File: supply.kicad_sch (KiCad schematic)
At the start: 138 parts, among them J10002 PinHeader_1x3_P2.54mm_Drill1.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, J1001 BarrelJack_3167288, Q10001 BSS138PW, Q1001 SI7613DN-T1-GE3, Q1002 BSS138PW, SW1001 SW_CVS-02B, U10001 NCP718BSN330T1G, U10002 MPM54304GMN, U10003 MPM54304GMN, U10004 MAX16150A_SOT, U10006 LM3880, U10007 MP8869S, U10008 XC6230H001ER-G, U10009 MAX812REUS+T, U1001 LTC4412IS6, U10010 PAC1954T-E_VQFN, U10011 PAC1954T-E_VQFN

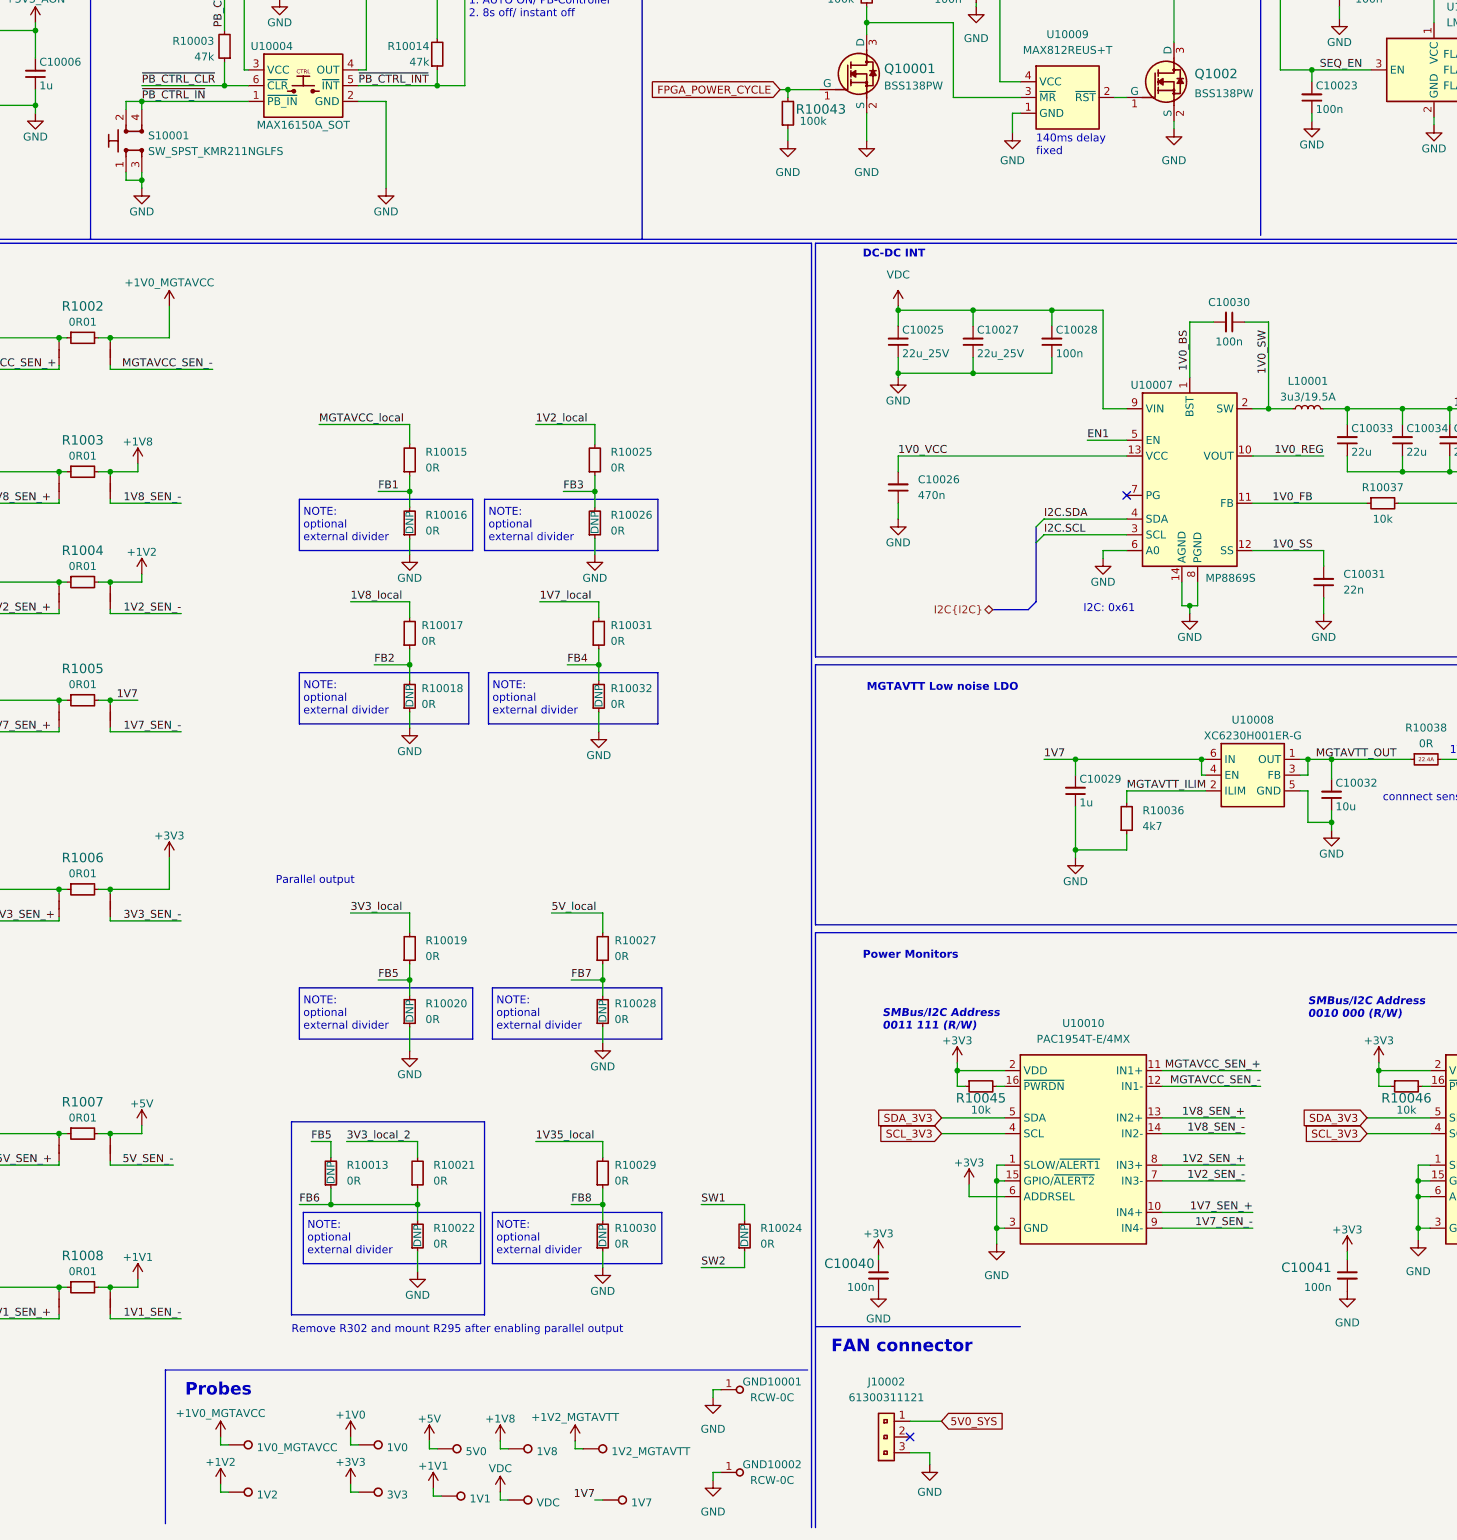
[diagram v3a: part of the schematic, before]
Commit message: Sync Supply sheet with PCB
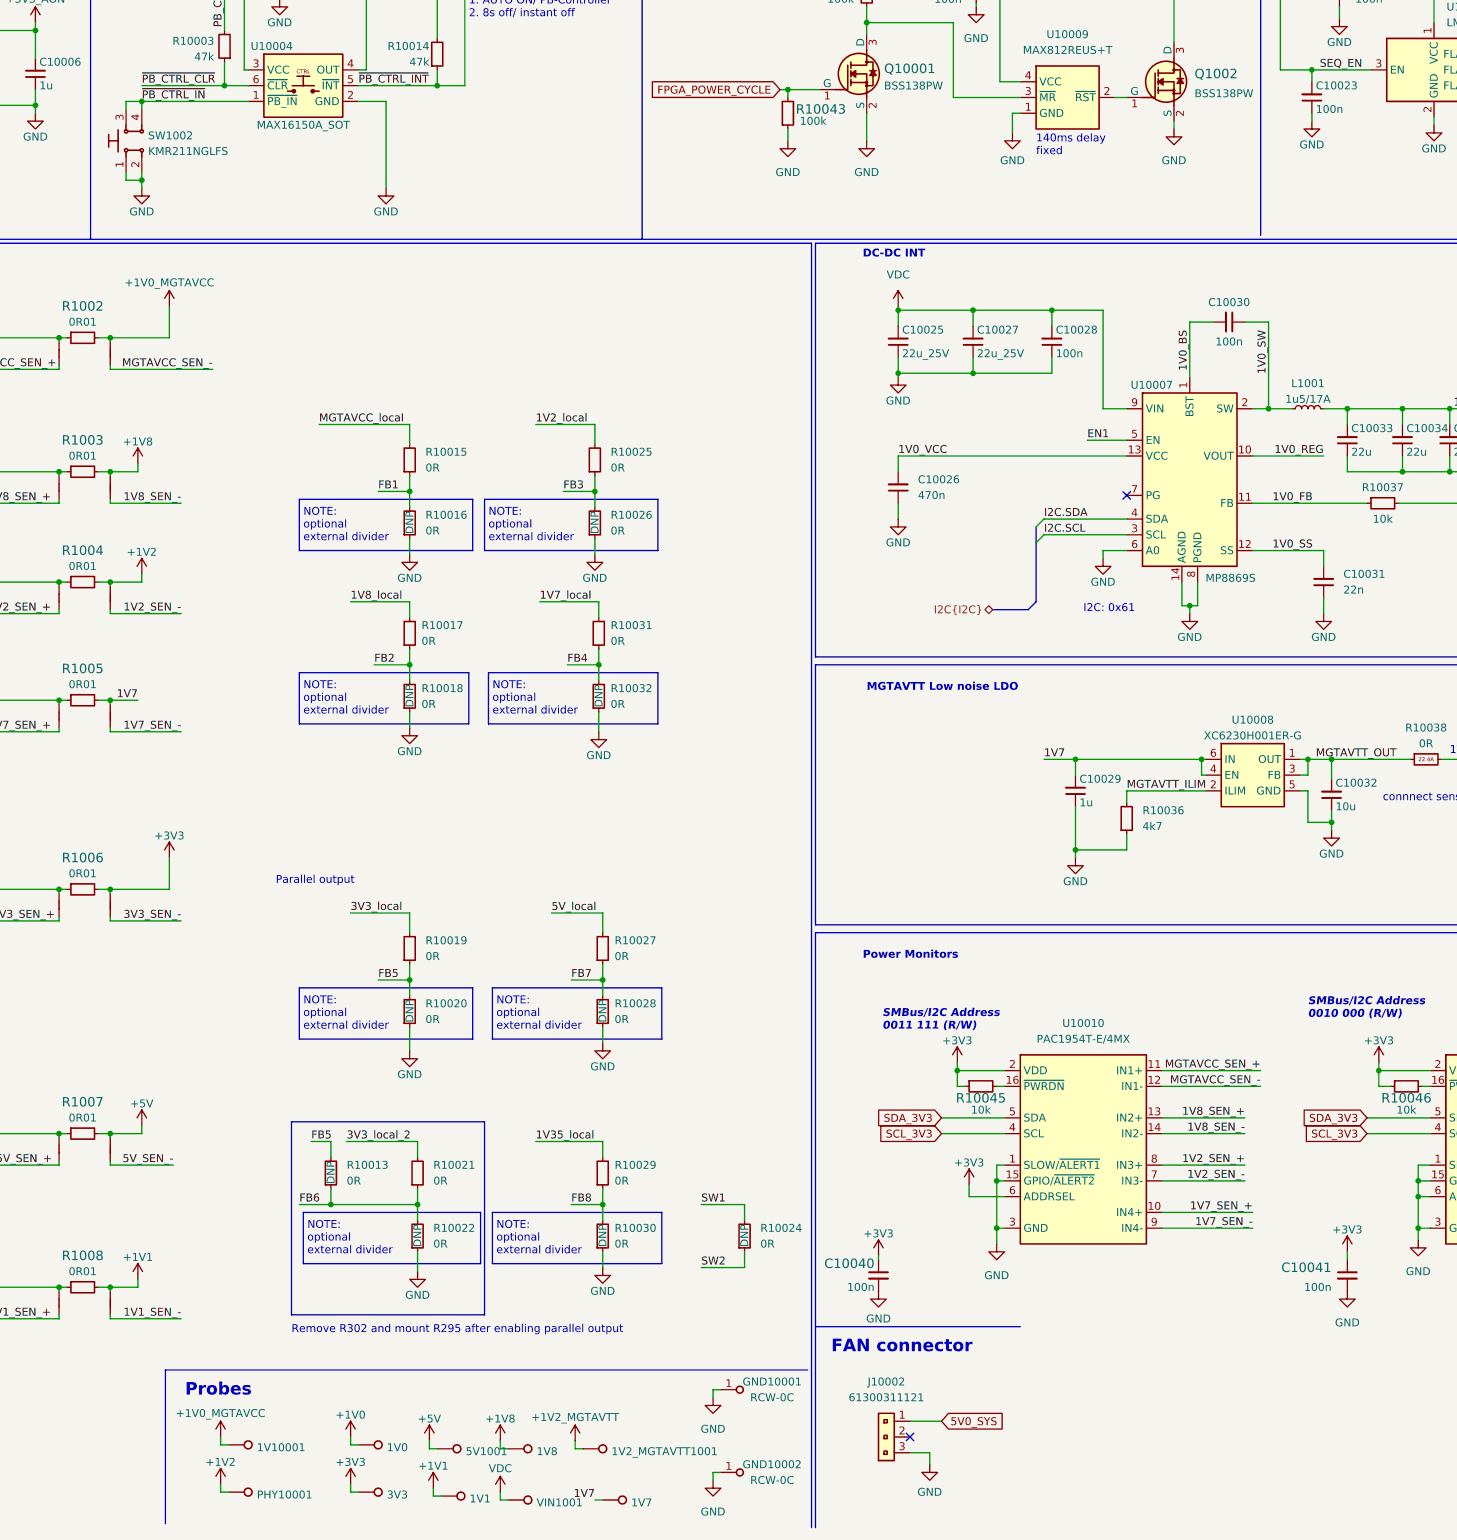
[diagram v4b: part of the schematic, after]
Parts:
- removed L10001: SRP6050CA-1R5M, K410T-devboard-footprints:Bourns-SRP6050CA, symbol K410T-devboard:SRP6050CA-1R5M
- removed S10001: SW_SPST_KMR211NGLFS, K410T-devboard-footprints:SW_SPST_4.2x2.8, symbol K410T-devboard:SW_SPST_KMR211NGLFS
- added L1001: L_1u5_17A_Bourns-SRP6050CA, antmicro-footprints:L_Bourns-SRP6050CA, symbol antmicroFixedInductors:L_1u5_17A_Bourns-SRP6050CA
- added SW1002: SW_KMR211NGLFS_SMD, antmicro-footprints:SW_KMR211NGLFS_SMD, symbol antmicroPushbuttonSwitches:SW_KMR211NGLFS_SMD
- renumbered 1V0_MGTAVCC to 1V10001, 1V2_MGTAVTT to 1V2_MGTAVTT1001, 5V0 to 5V1001, 1V2 to PHY10001, VDC to VIN1001
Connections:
- net 1V0_REG: now also L1001.2
- net 1V0_SW: now also L1001.1
- net GND: now also SW1002.1, SW1002.2
- net ~{PB_CTRL_IN}: now also SW1002.3, SW1002.4
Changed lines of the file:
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@@
   (symbol (lib_id "data-center-rdimm-ddr4-tester:TP_1mm_SMD") (at 205.74 272.415 0) (unit 1)
     (in_bom yes) (on_board yes) (fields_autoplaced)
-    (property "Reference" "5V0" (id 0) (at 210.312 272.8488 0)
+    (property "Reference" "5V1001" (id 0) (at 210.312 272.8488 0)
       (effects (font (size 1.27 1.27)) (justify left))
     )
@@
   (symbol (lib_id "data-center-rdimm-ddr4-tester:TP_1mm_SMD") (at 172.085 279.4 0) (unit 1)
     (in_bom yes) (on_board yes) (fields_autoplaced)
-    (property "Reference" "1V2" (id 0) (at 176.657 279.8338 0)
+    (property "Reference" "PHY10001" (id 0) (at 176.657 279.8338 0)
       (effects (font (size 1.27 1.27)) (justify left))
     )
@@
   (symbol (lib_id "data-center-rdimm-ddr4-tester:TP_1mm_SMD") (at 217.17 280.67 0) (unit 1)
     (in_bom yes) (on_board yes)
-    (property "Reference" "VDC" (id 0) (at 221.742 281.1038 0)
+    (property "Reference" "VIN1001" (id 0) (at 221.742 281.1038 0)
       (effects (font (size 1.27 1.27)) (justify left))
     )
@@
   (symbol (lib_id "data-center-rdimm-ddr4-tester:TP_1mm_SMD") (at 172.085 271.78 0) (unit 1)
     (in_bom yes) (on_board yes) (fields_autoplaced)
-    (property "Reference" "1V0_MGTAVCC" (id 0) (at 176.657 272.2138 0)
+    (property "Reference" "1V10001" (id 0) (at 176.657 272.2138 0)
       (effects (font (size 1.27 1.27)) (justify left))
     )
@@
     (pin "5")
   )
+  (symbol (lib_id "antmicroPushbuttonSwitches:SW_KMR211NGLFS_SMD") (at 155.575 66.675 90) (unit 1)
+    (in_bom yes) (on_board yes) (fields_autoplaced)
+    (property "Reference" "SW1002" (id 0) (at 159.131 60.7644 90)
+      (effects (font (size 1.27 1.27) (thickness 0.15)) (justify right))
+    )
+    (property "Value" "SW_KMR211NGLFS_SMD" (id 1) (at 163.195 41.275 0)
+      (effects (font (size 1.27 1.27) (thickness 0.15)) (justify left bottom) hide)
+    )
+    (property "Footprint" "antmicro-footprints:SW_KMR211NGLFS_SMD" (id 2) (at 165.735 41.275 0)
+      (effects (font (size 1.27 1.27) (thickness 0.15)) (justify left bottom) hide)
+    )
+    (property "Datasheet" "http://www.farnell.com/datasheets/2631211.pdf" (id 3) (at 168.275 41.275 0)
+      (effects (font (size 1.27 1.27) (thickness 0.15)) (justify left bottom) hide)
+    )
+    (property "MPN" "KMR211NGLFS" (id 4) (at 159.131 63.2881 90)
+      (effects (font (size 1.27 1.27) (thickness 0.15)) (justify right))
+    )
+    (property "Manufacturer" "C&K" (id 5) (at 170.815 41.275 0)
+      (effects (font (size 1.27 1.27) (thickness 0.15)) (justify left bottom) hide)
+    )
+    (property "Author" "Antmicro" (id 6) (at 173.355 41.275 0)
+      (effects (font (size 1.27 1.27) (thickness 0.15)) (justify left bottom) hide)
+    )
+    (property "License" "Apache-2.0" (id 7) (at 175.895 41.275 0)
+      (effects (font (size 1.27 1.27) (thickness 0.15)) (justify left bottom) hide)
+    )
+    (pin "1")
+    (pin "2")
+    (pin "3")
+    (pin "4")
+  )
   (symbol (lib_id "data-center-rdimm-ddr4-tester:GND") (at 352.425 247.015 0) (unit 1)
     (in_bom yes) (on_board yes) (fields_autoplaced)
@@
     (pin "2")
   )
-  (symbol (lib_id "K410T-devboard:SRP6050CA-1R5M") (at 343.535 104.775 0) (unit 1)
-    (in_bom yes) (on_board yes)
-    (property "Reference" "L10001" (id 0) (at 346.075 100.33 0))
-    (property "Value" "SRP6050CA-1R5M" (id 1) (at 357.505 107.315 0)
-      (effects (font (size 1.27 1.27) (thickness 0.15)) (justify left bottom) hide)
-    )
-    (property "Footprint" "K410T-devboard-footprints:Bourns-SRP6050CA" (id 2) (at 357.505 112.395 0)
-      (effects (font (size 1.27 1.27) (thickness 0.15)) (justify left bottom) hide)
-    )
-    (property "Datasheet" "https://www.bourns.com/docs/product-datasheets/srp6030va.pdf" (id 3) (at 357.505 114.935 0)
-      (effects (font (size 1.27 1.27) (thickness 0.15)) (justify left bottom) hide)
-    )
-    (property "Manufacturer" "Bourns" (id 4) (at 357.505 117.475 0)
-      (effects (font (size 1.27 1.27) (thickness 0.15)) (justify left bottom) hide)
-    )
-    (property "MPN" "SRP6050CA-1R5M" (id 5) (at 357.505 120.015 0)
-      (effects (font (size 1.27 1.27) (thickness 0.15)) (justify left bottom) hide)
-    )
-    (property "Size" "6.6x6.6" (id 7) (at 357.505 127.635 0)
-      (effects (font (size 1.27 1.27) (thickness 0.15)) (justify left bottom) hide)
-    )
-    (property "Val" "3u3/19.5A" (id 8) (at 346.075 102.87 0)
-      (effects (font (size 1.27 1.27) (thickness 0.15)))
-    )
-    (property "ISat" "" (id 9) (at 357.505 121.285 0)
-      (effects (font (size 1.27 1.27)) (justify left) hide)
-    )
-    (property "IMax" "" (id 10) (at 357.505 125.095 0)
-      (effects (font (size 1.27 1.27) (thickness 0.15)) (justify left bottom) hide)
-    )
-    (property "Author" "Antmicro" (id 11) (at 357.505 130.175 0)
-      (effects (font (size 1.27 1.27) (thickness 0.15)) (justify left bottom) hide)
-    )
-    (property "License" "Apache-2.0" (id 12) (at 357.505 132.715 0)
-      (effects (font (size 1.27 1.27) (thickness 0.15)) (justify left bottom) hide)
-    )
-    (pin "1")
-    (pin "2")
-  )
   (symbol (lib_id "data-center-rdimm-ddr4-tester:GND") (at 250.19 277.495 0) (mirror y) (unit 1)
     (in_bom yes) (on_board yes) (fields_autoplaced)
@@
   (symbol (lib_id "data-center-rdimm-ddr4-tester:TP_1mm_SMD") (at 229.235 272.415 0) (unit 1)
     (in_bom yes) (on_board yes) (fields_autoplaced)
-    (property "Reference" "1V2_MGTAVTT" (id 0) (at 233.807 272.8488 0)
+    (property "Reference" "1V2_MGTAVTT1001" (id 0) (at 233.807 272.8488 0)
       (effects (font (size 1.27 1.27)) (justify left))
     )
@@
     (pin "2")
   )
-  (symbol (lib_id "K410T-devboard:SW_SPST_KMR211NGLFS") (at 155.575 66.675 90) (unit 1)
-    (in_bom yes) (on_board yes) (fields_autoplaced)
-    (property "Reference" "S10001" (id 0) (at 159.131 60.7644 90)
-      (effects (font (size 1.27 1.27)) (justify right))
-    )
-    (property "Value" "SW_SPST_KMR211NGLFS" (id 1) (at 159.131 63.2947 90)
-      (effects (font (size 1.27 1.27) (thickness 0.15)) (justify right))
-    )
-    (property "Footprint" "K410T-devboard-footprints:SW_SPST_4.2x2.8" (id 2) (at 163.195 41.275 0)
-      (effects (font (size 1.27 1.27) (thickness 0.15)) (justify left bottom) hide)
-    )
-    (property "Datasheet" "http://www.farnell.com/datasheets/2631211.pdf" (id 3) (at 165.735 41.275 0)
-      (effects (font (size 1.27 1.27) (thickness 0.15)) (justify left bottom) hide)
-    )
-    (property "MPN" "KMR211NGLFS" (id 4) (at 168.275 41.275 0)
-      (effects (font (size 1.27 1.27) (thickness 0.15)) (justify left bottom) hide)
-    )
-    (property "Manufacturer" "C&K" (id 5) (at 170.815 41.275 0)
-      (effects (font (size 1.27 1.27) (thickness 0.15)) (justify left bottom) hide)
-    )
-    (property "Author" "Antmicro" (id 6) (at 173.355 41.275 0)
-      (effects (font (size 1.27 1.27) (thickness 0.15)) (justify left bottom) hide)
-    )
-    (property "License" "Apache-2.0" (id 7) (at 175.895 41.275 0)
-      (effects (font (size 1.27 1.27) (thickness 0.15)) (justify left bottom) hide)
-    )
-    (pin "1")
-    (pin "2")
-    (pin "3")
-    (pin "4")
-  )
   (symbol (lib_id "antmicroResistors0402:R_0R_0402") (at 232.41 204.47 90) (unit 1)
     (in_bom yes) (on_board yes)
@@
     )
     (pin "1")
+    (pin "2")
+  )
+  (symbol (lib_id "antmicroFixedInductors:L_1u5_17A_Bourns-SRP6050CA") (at 343.535 104.775 0) (unit 1)
+    (in_bom yes) (on_board yes) (fields_autoplaced)
+    (property "Reference" "L1001" (id 0) (at 346.075 100.709 0)
+      (effects (font (size 1.27 1.27) (thickness 0.15)))
+    )
+    (property "Value" "L_1u5_17A_Bourns-SRP6050CA" (id 1) (at 357.505 107.315 0)
+      (effects (font (size 1.27 1.27) (thickness 0.15)) (justify left bottom) hide)
+    )
+    (property "Footprint" "antmicro-footprints:L_Bourns-SRP6050CA" (id 2) (at 357.505 112.395 0)
+      (effects (font (size 1.27 1.27) (thickness 0.15)) (justify left bottom) hide)
+    )
+    (property "Datasheet" "https://www.bourns.com/docs/Product-Datasheets/SRP6050CA.pdf" (id 3) (at 357.505 114.935 0)
+      (effects (font (size 1.27 1.27) (thickness 0.15)) (justify left bottom) hide)
+    )
+    (property "Val" "1u5/17A" (id 4) (at 346.075 103.2327 0)
+      (effects (font (size 1.27 1.27) (thickness 0.15)))
+    )
+    (property "Manufacturer" "Bourns" (id 5) (at 357.505 117.475 0)
+      (effects (font (size 1.27 1.27) (thickness 0.15)) (justify left bottom) hide)
+    )
+    (property "MPN" "SRP6050CA-1R5M" (id 6) (at 357.505 120.015 0)
+      (effects (font (size 1.27 1.27) (thickness 0.15)) (justify left bottom) hide)
+    )
+    (property "ISat" "19.5 A" (id 7) (at 357.505 121.285 0)
+      (effects (font (size 1.27 1.27)) (justify left) hide)
+    )
+    (property "IMax" "17 A" (id 8) (at 357.505 125.095 0)
+      (effects (font (size 1.27 1.27) (thickness 0.15)) (justify left bottom) hide)
+    )
+    (property "Size" "6.6x6.6" (id 9) (at 357.505 127.635 0)
+      (effects (font (size 1.27 1.27) (thickness 0.15)) (justify left bottom) hide)
+    )
+    (property "Author" "Antmicro" (id 10) (at 357.505 130.175 0)
+      (effects (font (size 1.27 1.27) (thickness 0.15)) (justify left bottom) hide)
+    )
+    (property "License" "Apache-2.0" (id 11) (at 357.505 132.715 0)
+      (effects (font (size 1.27 1.27) (thickness 0.15)) (justify left bottom) hide)
+    )
+    (pin "1")

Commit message: Add power supply layout
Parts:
- renumbered 1V0 to 1V10002, 1V1 to 1V10003, 1V8 to 1V10004, 1V7 to 1V10005, 1V2_MGTAVTT1001 to 1V2_MGTAVTT10001, 3V3 to 3V10001, 5V1001 to 5V10001, C1001 to C10001, C1002 to C10002, C10002 to C10003, C10003 to C10004, C10004 to C10005, C10005 to C10006, C1003 to C10009, C10001 to C10010, C10009 to C10011, C10010 to C10012, C10011 to C10013, C10012 to C10014, C10013 to C10015, C10014 to C10016, C10015 to C10017, C10016 to C10018, C10017 to C10019, C10018 to C10020, C10019 to C10021, C10020 to C10022, C10006 to C10023, C10021 to C10024, C10040 to C10025, C10025 to C10026, C10026 to C10027, C10027 to C10028, C10039 to C10029, C10028 to C10030, C10029 to C10031, C10030 to C10032, C10023 to C10033, C10031 to C10034, C10032 to C10035, C10024 to C10036, C10033 to C10037, C10041 to C10038, C10034 to C10039, C10035 to C10040, C10036 to C10041, C10037 to C10042, D1001 to D10001, D1002 to D10002, F1001 to F10001, J1001 to J10001, L1001 to L10001, NT1001 to NT10001, NT1002 to NT10002, NT1003 to NT10003, NT1004 to NT10004, NT1005 to NT10005, NT1006 to NT10006, NT1007 to NT10007, NT1008 to NT10008, NT1009 to NT10009, NT1010 to NT10010, NT1011 to NT10011, NT1012 to NT10012, NT1013 to NT10013, NT1014 to NT10014, Q1001 to Q10001, Q10001 to Q10002, Q1002 to Q10003, R1001 to R10001, R1002 to R10002, R1003 to R10003, R1004 to R10004, R1005 to R10005, R1006 to R10006, R1007 to R10007, R1008 to R10008, R10003 to R10009, R10013 to R10010, R10015 to R10011, R10016 to R10012, R10017 to R10013, R10018 to R10014, R10019 to R10015, R10020 to R10016, R10021 to R10017, R10022 to R10018, R10014 to R10019, R10025 to R10020, R10026 to R10021, R10031 to R10022, R10032 to R10023, R10027 to R10024, R10028 to R10025, R10029 to R10026, R10030 to R10027, R10024 to R10028, R10043 to R10029, R10044 to R10030, R10045 to R10031, R10036 to R10032, R10037 to R10033, R10046 to R10034, R10038 to R10035, R10033 to R10036, R10039 to R10037, R10040 to R10038, R10034 to R10039, R10041 to R10040, R10042 to R10041, R10035 to R10042, SW1002 to SW10001, SW1001 to SW10002, U1001 to U10001, U10001 to U10004, U10004 to U10005, U10010 to U10006, U10009 to U10007, U10007 to U10008, U10008 to U10009, U10011 to U10010, U10006 to U10011, VIN1001 to VIN10001

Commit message: Update PCIe label names and add 12V Aux circuit
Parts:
- added C?: C_100n_0402, antmicro-footprints:C_0402_1005Metric, symbol antmicroCapacitors0402:C_100n_0402
- D1002: renamed from D10002; DNP DNP -> (none)
- renumbered 1V10002 to 1V0, 1V10003 to 1V1, 1V2_MGTAVTT10001 to 1V2_MGTAVTT1001, 1V10005 to 1V7, 1V10004 to 1V8, 3V10001 to 3V3, 5V10001 to 5V1001, C10010 to C10001, C10003 to C10002, C10004 to C10003, C10005 to C10004, C10006 to C10005, C10023 to C10006, C10011 to C10009, C10001 to C1001, C10012 to C10010, C10013 to C10011, C10014 to C10012, C10015 to C10013, C10016 to C10014, C10017 to C10015, C10018 to C10016, C10019 to C10017, C10020 to C10018, C10021 to C10019, C10002 to C1002, C10022 to C10020, C10024 to C10021, C10033 to C10023, C10036 to C10024, C10026 to C10025, C10027 to C10026, C10028 to C10027, C10030 to C10028, C10031 to C10029, C10009 to C1003, C10032 to C10030, C10034 to C10031, C10035 to C10032, C10037 to C10033, C10039 to C10034, C10040 to C10035, C10041 to C10036, C10042 to C10037, C10029 to C10039, C10025 to C10040, C10038 to C10041, D10001 to D1001, F10001 to F1001, J10001 to J1001, L10001 to L1001, NT10001 to NT1001, NT10002 to NT1002, NT10003 to NT1003, NT10004 to NT1004, NT10005 to NT1005, NT10006 to NT1006, NT10007 to NT1007, NT10008 to NT1008, NT10009 to NT1009, NT10010 to NT1010, NT10011 to NT1011, NT10012 to NT1012, NT10013 to NT1013, NT10014 to NT1014, Q10002 to Q10001, Q10001 to Q1001, Q10003 to Q1002, R10009 to R10003, R10001 to R1001, R10010 to R10013, R10019 to R10014, R10011 to R10015, R10012 to R10016, R10013 to R10017, R10014 to R10018, R10015 to R10019, R10002 to R1002, R10016 to R10020, R10017 to R10021, R10018 to R10022, R10028 to R10024, R10020 to R10025, R10021 to R10026, R10024 to R10027, R10025 to R10028, R10026 to R10029, R10003 to R1003, R10027 to R10030, R10022 to R10031, R10023 to R10032, R10036 to R10033, R10039 to R10034, R10042 to R10035, R10032 to R10036, R10033 to R10037, R10035 to R10038, R10037 to R10039, R10004 to R1004, R10038 to R10040, R10040 to R10041, R10041 to R10042, R10029 to R10043, R10030 to R10044, R10031 to R10045, R10034 to R10046, R10005 to R1005, R10006 to R1006, R10007 to R1007, R10008 to R1008, SW10002 to SW1001, SW10001 to SW1002, U10004 to U10001, U10005 to U10004, U10011 to U10006, U10008 to U10007, U10009 to U10008, U10007 to U10009, U10001 to U1001, U10006 to U10010, U10010 to U10011, VIN10001 to VIN1001
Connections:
- net GND: now also C?.1
- net at C1001.2, D1001.2 (A), D1002.2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: no longer C1002.2, Q1001.5 (D), U1001.1 (IN)
- new net 12V_PCIE: C1002.2, C?.2, Q1001.5 (D), U1001.1 (IN)
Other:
- note added: "DC_PWR_AUX"
- note added: "PCIe_PWR_default"
- note added: "Power source"
- note removed: "DC JACK"
- moved on the sheet: C1001, C1002, C1003, D1001, D1002, F1001, J1001, Q1001, U1001
